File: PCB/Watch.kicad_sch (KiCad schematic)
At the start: 53 parts, among them J1 USB_C_Receptacle_USB2.0_14P, Q1 2N3906, Q2 2N3906, Q3 2N3906, Q4 2N3906, SW1 SW_Push, SW3 SW_Push, SW4 SW_Push, U1 MCP73831-2-OT, U2 TPS63900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

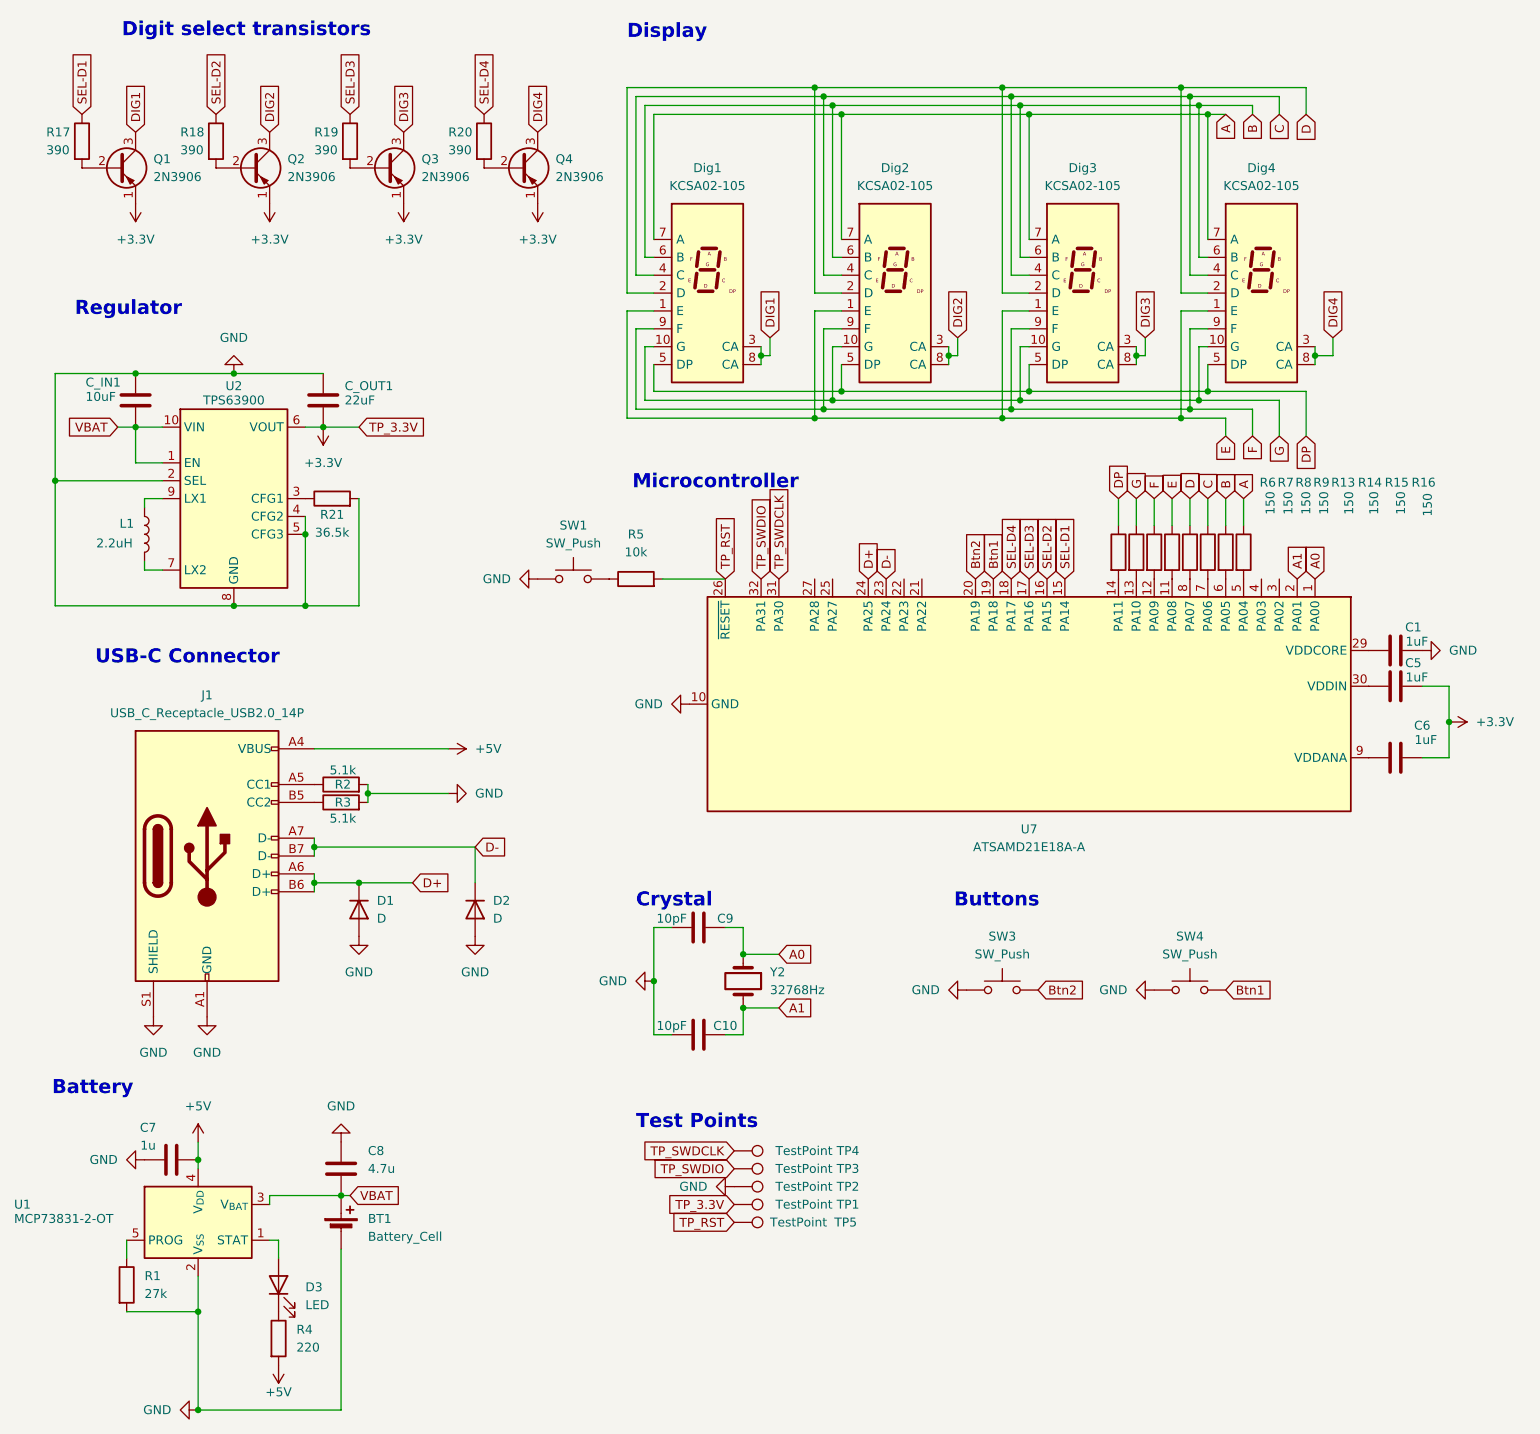
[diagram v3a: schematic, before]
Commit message: Fix regulator and voltage issue, replace inductor with LED
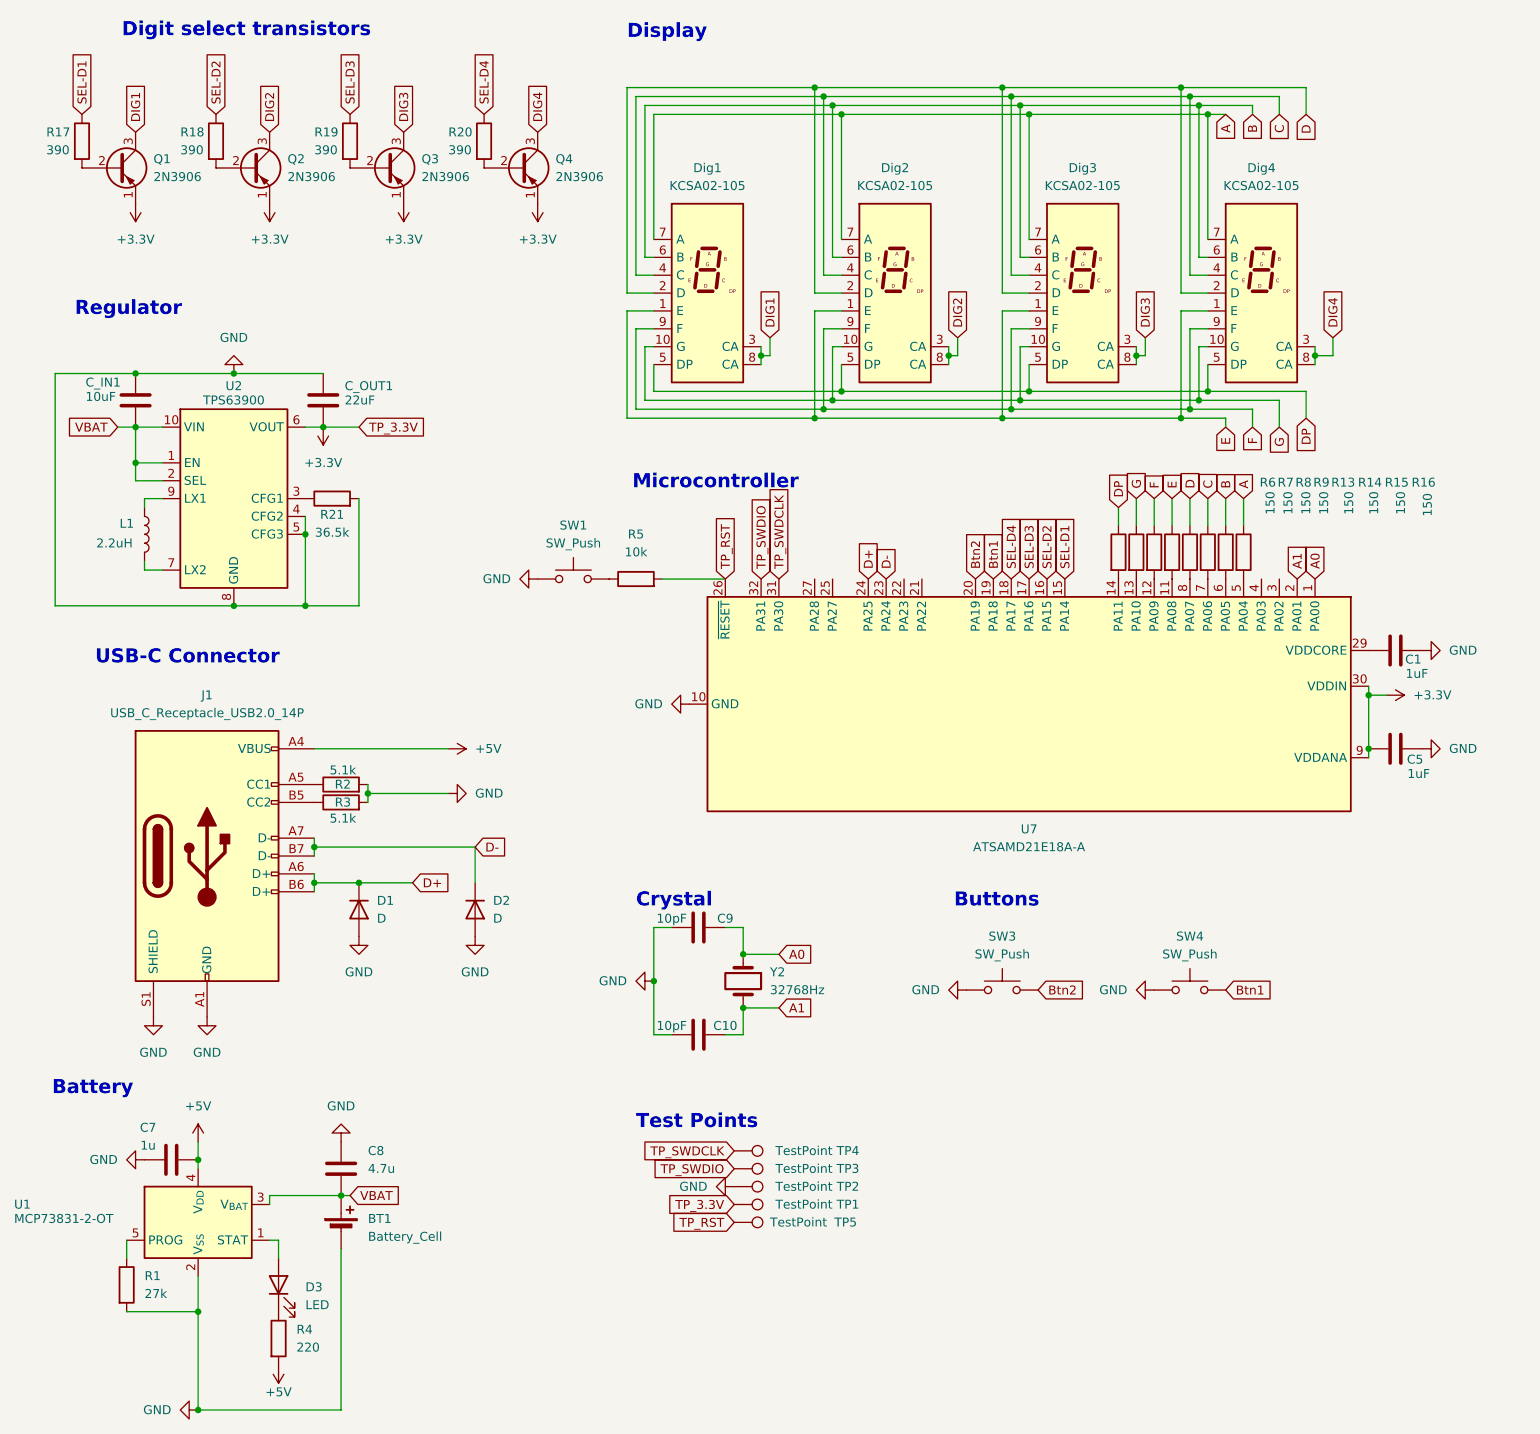
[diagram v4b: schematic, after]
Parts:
- removed C6: 1uF, Capacitor_SMD:C_0402_1005Metric, symbol Device:C
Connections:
- net +3.3V: now also C5.1, U7.30 (VDDIN), U7.9 (VDDANA); no longer C5.2
- net GND: now also C5.2; no longer U2.2 (SEL)
- net VBAT: now also U2.2 (SEL)
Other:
- moved on the sheet: C5
